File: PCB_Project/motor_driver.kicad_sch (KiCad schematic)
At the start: 6 parts

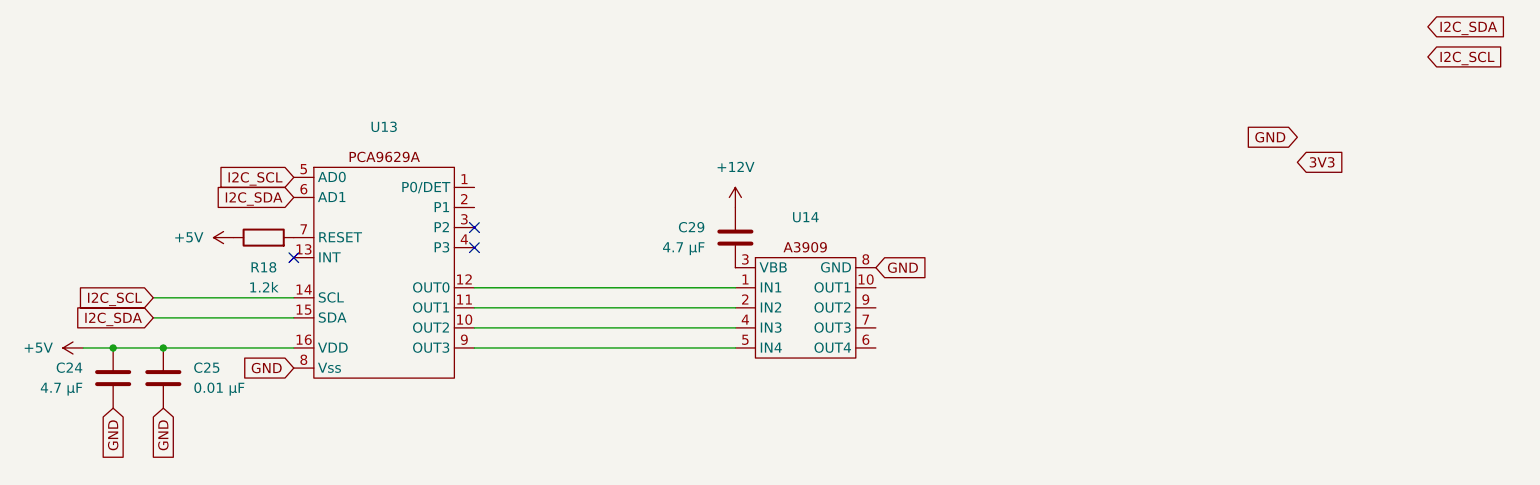
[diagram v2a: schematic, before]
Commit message: added the header
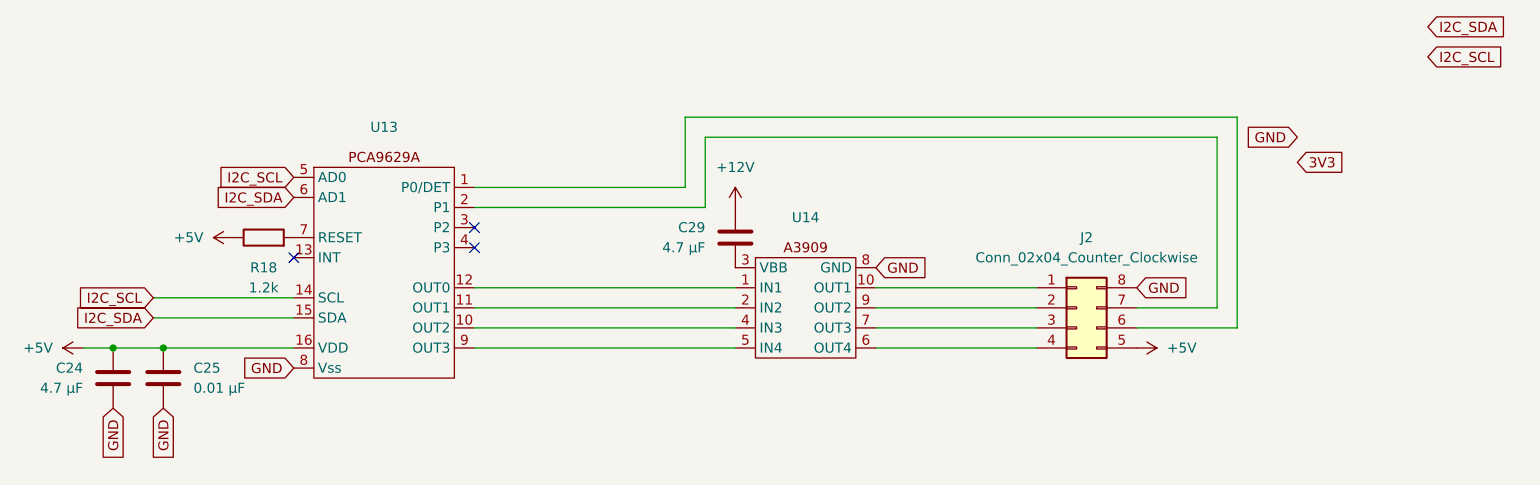
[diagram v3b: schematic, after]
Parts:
- added J2: Conn_02x04_Counter_Clockwise, symbol Connector_Generic:Conn_02x04_Counter_Clockwise
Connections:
- net +5V: now also J2.5 (Pin_5)
- net GND: now also J2.8 (Pin_8)
- net at U13.1 (P0/DET): now also J2.6 (Pin_6)
- net at U13.2 (P1): now also J2.7 (Pin_7)
- net at U14.10 (OUT1): now also J2.1 (Pin_1)
- net at U14.6 (OUT4): now also J2.4 (Pin_4)
- net at U14.7 (OUT3): now also J2.3 (Pin_3)
- net at U14.9 (OUT2): now also J2.2 (Pin_2)
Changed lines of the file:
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@@
   (no_connect (at 93.98 72.39))
   (no_connect (at 93.98 69.85))
+  (wire (pts (xy 93.98 67.31) (xy 123.19 67.31))
+    (stroke (width 0) (type default))
+  )
   (wire (pts (xy 53.34 78.74) (xy 71.12 78.74))
     (stroke (width 0) (type default))
@@
     (stroke (width 0) (type default))
   )
+  (wire (pts (xy 187.96 58.42) (xy 187.96 80.01))
+    (stroke (width 0) (type default))
+  )
+  (wire (pts (xy 187.96 80.01) (xy 177.8 80.01))
+    (stroke (width 0) (type default))
+  )
+  (wire (pts (xy 190.5 55.88) (xy 190.5 82.55))
+    (stroke (width 0) (type default))
+  )
   (wire (pts (xy 53.34 81.28) (xy 71.12 81.28))
     (stroke (width 0) (type default))
   )
+  (wire (pts (xy 120.65 55.88) (xy 190.5 55.88))
+    (stroke (width 0) (type default))
+  )
+  (wire (pts (xy 144.78 80.01) (xy 165.1 80.01))
+    (stroke (width 0) (type default))
+  )
+  (wire (pts (xy 123.19 67.31) (xy 123.19 58.42))
+    (stroke (width 0) (type default))
+  )
   (wire (pts (xy 44.45 85.09) (xy 48.26 85.09))
     (stroke (width 0) (type default))
   )
+  (wire (pts (xy 93.98 64.77) (xy 120.65 64.77))
+    (stroke (width 0) (type default))
+  )
   (wire (pts (xy 54.61 85.09) (xy 71.12 85.09))
     (stroke (width 0) (type default))
   )
+  (wire (pts (xy 144.78 82.55) (xy 165.1 82.55))
+    (stroke (width 0) (type default))
+  )
   (wire (pts (xy 93.98 80.01) (xy 127 80.01))
     (stroke (width 0) (type default))
   )
+  (wire (pts (xy 144.78 77.47) (xy 165.1 77.47))
+    (stroke (width 0) (type default))
+  )
+  (wire (pts (xy 123.19 58.42) (xy 187.96 58.42))
+    (stroke (width 0) (type default))
+  )
+  (wire (pts (xy 190.5 82.55) (xy 177.8 82.55))
+    (stroke (width 0) (type default))
+  )
+  (wire (pts (xy 120.65 64.77) (xy 120.65 55.88))
+    (stroke (width 0) (type default))
+  )
   (wire (pts (xy 93.98 85.09) (xy 127 85.09))
     (stroke (width 0) (type default))
@@
     (stroke (width 0) (type default))
   )
+  (wire (pts (xy 144.78 85.09) (xy 165.1 85.09))
+    (stroke (width 0) (type default))
+  )
   (global_label "GND" (shape input) (at 71.12 87.63 180) (fields_autoplaced)
     (effects (font (size 1.27 1.27)) (justify right))
@@
     (property "Intersheetrefs" "${INTERSHEET_REFS}" (at 48.26 99.5657 90)
       (effects (font (size 1.27 1.27)) (justify right) hide)
+    )
+  )
+  (global_label "GND" (shape input) (at 177.8 77.47 0) (fields_autoplaced)
+    (effects (font (size 1.27 1.27)) (justify left))
+    (property "Intersheetrefs" "${INTERSHEET_REFS}" (at 184.6557 77.47 0)
+      (effects (font (size 1.27 1.27)) (justify left) hide)
     )
   )
@@
         )
       )
+    )
+  )
+  (symbol (lib_id "power:+5V") (at 177.8 85.09 270) (unit 1)
+    (in_bom yes) (on_board yes) (dnp no) (fields_autoplaced)
+    (property "Reference" "#PWR014" (at 173.99 85.09 0)
+      (effects (font (size 1.27 1.27)) hide)
+    )
+    (property "Value" "+5V" (at 181.61 85.09 90)
+      (effects (font (size 1.27 1.27)) (justify left))
+    )
+    (property "Footprint" "" (at 177.8 85.09 0)
+      (effects (font (size 1.27 1.27)) hide)
+    )
+    (property "Datasheet" "" (at 177.8 85.09 0)
+      (effects (font (size 1.27 1.27)) hide)
+    )
+    (pin "1")
+    (instances
+      (project "PCB_Project"
+        (path "/3dbd20c6-0b48-4a74-89bd-dd4c54711bfb/8bf501f3-4a83-420c-953d-b9bdabd30bb8"
+          (reference "#PWR014") (unit 1)
+        )
+      )
+    )
+  )
+  (symbol (lib_id "Connector_Generic:Conn_02x04_Counter_Clockwise") (at 170.18 80.01 0) (unit 1)
+    (in_bom yes) (on_board yes) (dnp no) (fields_autoplaced)
+    (property "Reference" "J2" (at 171.45 71.12 0)
+      (effects (font (size 1.27 1.27)))
+    )
+    (property "Value" "Conn_02x04_Counter_Clockwise" (at 171.45 73.66 0)
+      (effects (font (size 1.27 1.27)))
+    )
+    (property "Footprint" "" (at 170.18 80.01 0)
+      (effects (font (size 1.27 1.27)) hide)
+    )
+    (property "Datasheet" "~" (at 170.18 80.01 0)
+      (effects (font (size 1.27 1.27)) hide)
+    )
+    (pin "3")
+    (pin "6")
+    (pin "1")
+    (pin "5")
+    (pin "4")
+    (pin "2")
+    (pin "8")
+    (pin "7")
+    (instances
+      (project "PCB_Project"
+        (path "/3dbd20c6-0b48-4a74-89bd-dd4c54711bfb/8bf501f3-4a83-420c-953d-b9bdabd30bb8"
+          (reference "J2") (unit 1)
+        )
+      )

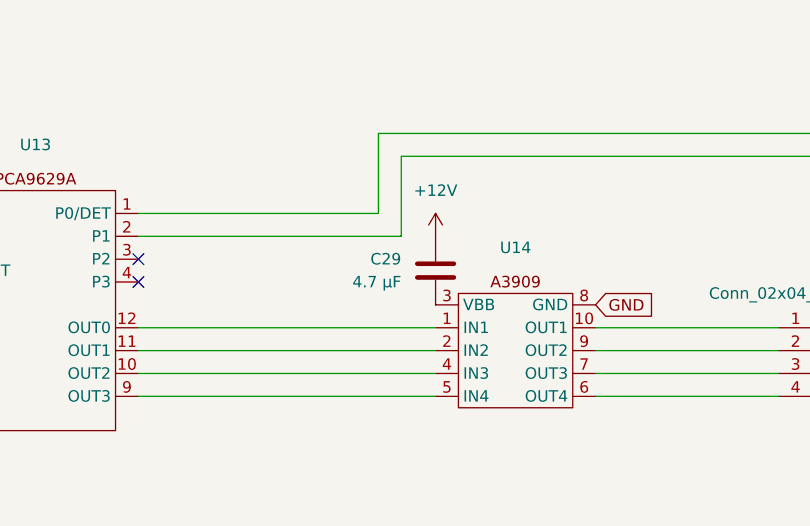
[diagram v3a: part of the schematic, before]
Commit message: the filter cap does not go between the voltage rail and the input pin
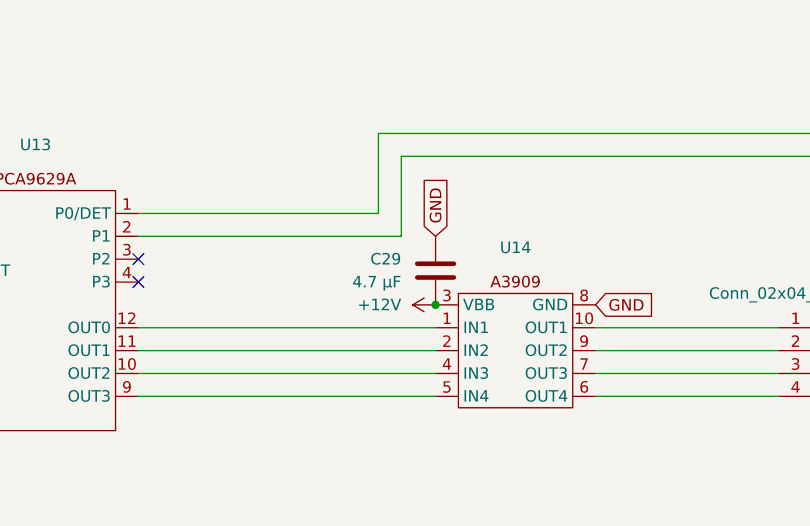
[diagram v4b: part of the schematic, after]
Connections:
- net +12V: now also C29.1, U14.3 (VBB); no longer C29.2
- net GND: now also C29.2
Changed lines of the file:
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@@
   (junction (at 48.26 85.09) (diameter 0) (color 0 0 0 0)
+  )
+  (junction (at 127 74.93) (diameter 0) (color 0 0 0 0)
   )
   (no_connect (at 71.12 73.66))
@@
     (effects (font (size 1.27 1.27)) (justify left))
     (property "Intersheetrefs" "${INTERSHEET_REFS}" (at 225.1747 48.26 0)
+      (effects (font (size 1.27 1.27)) (justify left) hide)
+    )
+  )
+  (global_label "GND" (shape input) (at 127 67.31 90) (fields_autoplaced)
+    (effects (font (size 1.27 1.27)) (justify left))
+    (property "Intersheetrefs" "${INTERSHEET_REFS}" (at 127 60.4543 90)
       (effects (font (size 1.27 1.27)) (justify left) hide)
     )
@@
     )
   )
-  (symbol (lib_id "power:+12V") (at 127 67.31 0) (unit 1)
+  (symbol (lib_id "power:+12V") (at 127 74.93 90) (unit 1)
     (in_bom yes) (on_board yes) (dnp no) (fields_autoplaced)
-    (property "Reference" "#PWR025" (at 127 71.12 0)
-      (effects (font (size 1.27 1.27)) hide)
-    )
-    (property "Value" "+12V" (at 127 62.23 0)
-      (effects (font (size 1.27 1.27)))
-    )
-    (property "Footprint" "" (at 127 67.31 0)
-      (effects (font (size 1.27 1.27)) hide)
-    )
-    (property "Datasheet" "" (at 127 67.31 0)
+    (property "Reference" "#PWR015" (at 130.81 74.93 0)
+      (effects (font (size 1.27 1.27)) hide)
+    )
+    (property "Value" "+12V" (at 123.19 74.93 90)
+      (effects (font (size 1.27 1.27)) (justify left))
+    )
+    (property "Footprint" "" (at 127 74.93 0)
+      (effects (font (size 1.27 1.27)) hide)
+    )
+    (property "Datasheet" "" (at 127 74.93 0)
       (effects (font (size 1.27 1.27)) hide)
     )
@@
       (project "PCB_Project"
         (path "/3dbd20c6-0b48-4a74-89bd-dd4c54711bfb/8bf501f3-4a83-420c-953d-b9bdabd30bb8"
-          (reference "#PWR025") (unit 1)
+          (reference "#PWR015") (unit 1)
         )
       )
